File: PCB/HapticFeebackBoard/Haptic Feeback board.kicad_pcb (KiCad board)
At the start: 2 copper layers, 46 x 41 mm, 14 parts, among them J1 1769, J2 Conn_01x02, J3 Conn_01x02, J4 Conn_01x02, Q1 2N7002E, SW1 PTS526 SM15 SMTR2 LFS

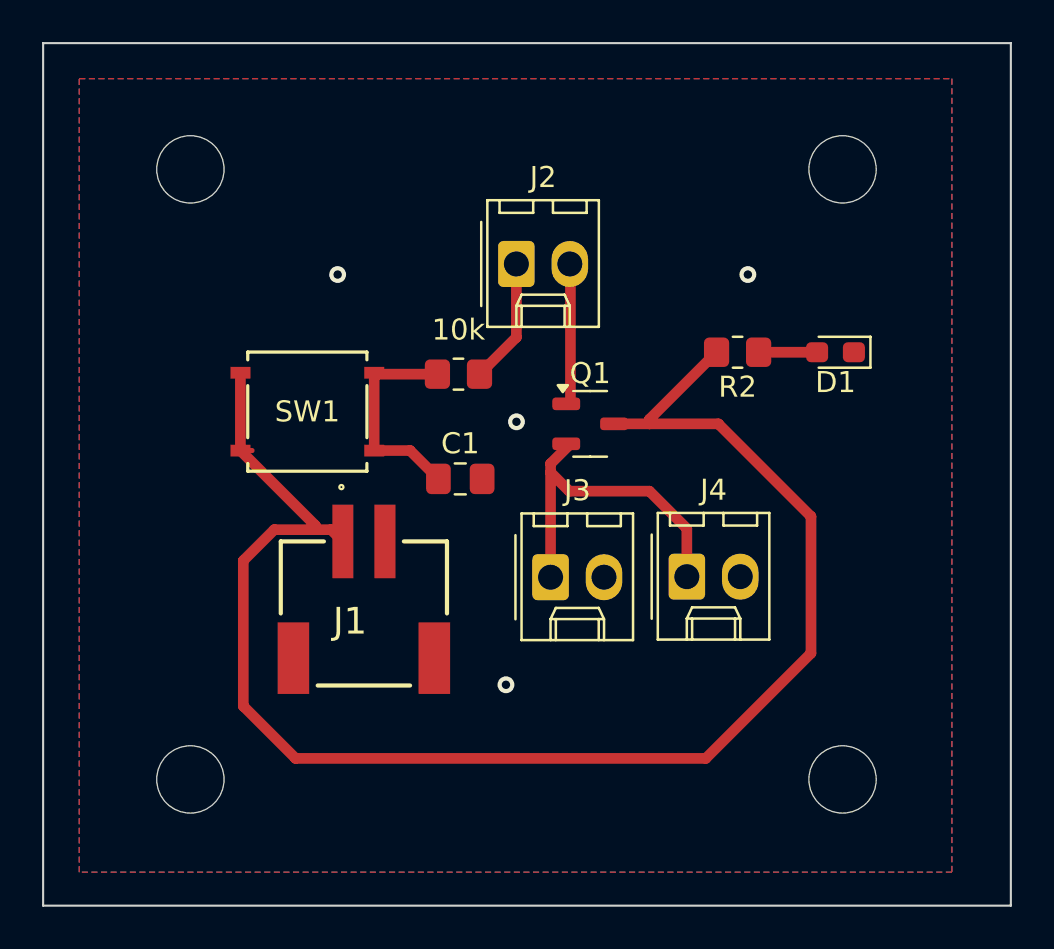
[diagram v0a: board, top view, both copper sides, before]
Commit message: Updated Haptic Feedback Board
Changed motor to be connected to the drain rather than source
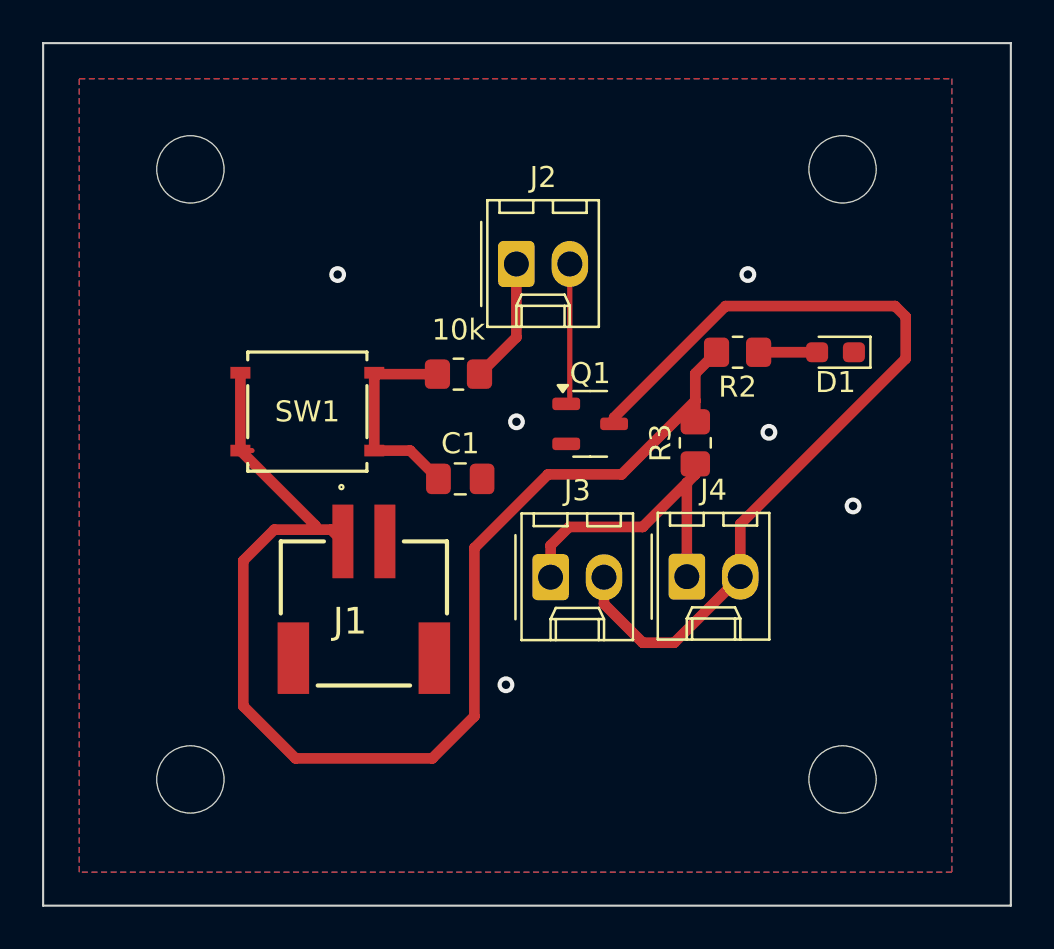
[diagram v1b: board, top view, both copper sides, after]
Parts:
- added R3: 10k, Resistor_SMD:R_0805_2012Metric_Pad1.20x1.40mm_HandSolder, F.Cu at (149.5, 96.0)
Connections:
- J3 pad 1: /Motor1 -> /Motor2
- J3 pad 2: GND -> /Motor1GND
- J4 pad 1: /Motor1 -> /Motor2
- J4 pad 2: GND -> /Motor1GND
- Q1 pad 2: /Motor1 -> GND
- Q1 pad 3: +3.3V -> /Motor1GND
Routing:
- net /Motor1GND: track 0.00 -> 42.0 mm
- net /Motor1: track 16.6 -> 0.00 mm
- net /Motor2: track 0.00 -> 14.7 mm
- net +3.3V: track 74.7 -> 59.9 mm
- net GND: vias 4 -> 6
